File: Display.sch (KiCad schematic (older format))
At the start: 16 parts, among them Q1 Q_NPN_BCE, Q2 Q_NPN_BCE, U1 74LS47, U5 DA56-11GWA

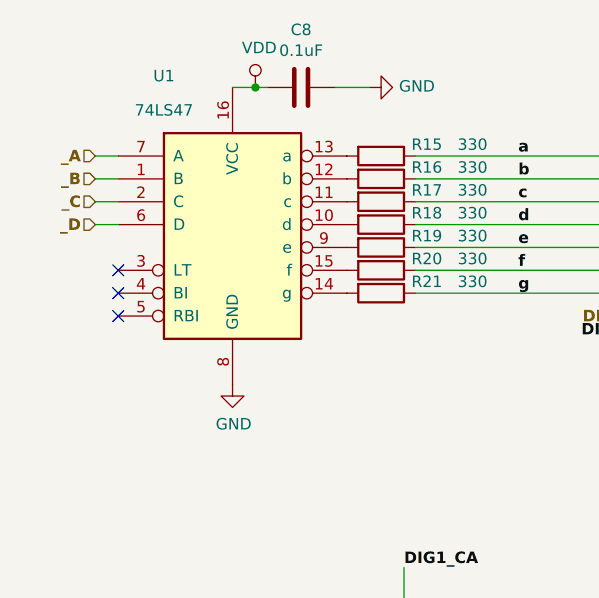
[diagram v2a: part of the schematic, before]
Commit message: Se agregan recomendaciones izq->dcha (In/Out), se Reorganiza jerarquía y bus de datos, se coloca graphics lines para indicar submodulos
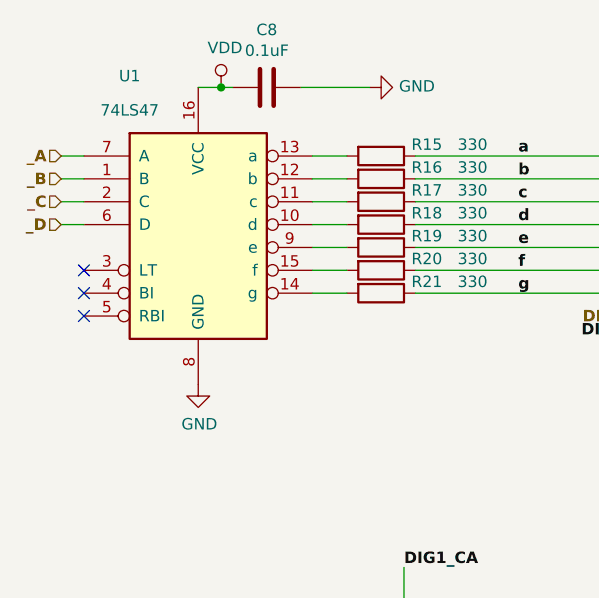
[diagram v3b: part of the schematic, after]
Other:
- moved on the sheet: C8, U1
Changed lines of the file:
@@
 $Descr A4 11693 8268
 encoding utf-8
-Sheet 4 4
+Sheet 2 4
 Title "Kit Development for MCU PIC"
 Date "2019-05-14"
@@
 L 74xx:74LS47 U1
 U 1 1 5CDD9840
-P 3950 2950
-F 0 "U1" H 3650 3600 50  0000 C CNN
-F 1 "74LS47" H 3650 3450 50  0000 C CNN
-F 2 "" H 3950 2950 50  0001 C CNN
-F 3 "http://www.ti.com/lit/gpn/sn74LS47" H 3950 2950 50  0001 C CNN
-	1    3950 2950
+P 3800 2950
+AR Path="/5CCF70C1/5CDD9840" Ref="U1"  Part="1"
+AR Path="/5CFF2978/5CDD9840" Ref="U?"  Part="1"
+AR Path="/5D021BAF/5CDD9840" Ref="U?"  Part="1"
+F 0 "U1" H 3500 3600 50  0000 C CNN
+F 1 "74LS47" H 3500 3450 50  0000 C CNN
+F 2 "" H 3800 2950 50  0001 C CNN
+F 3 "http://www.ti.com/lit/gpn/sn74LS47" H 3800 2950 50  0001 C CNN
+	1    3800 2950
 	1    0    0    -1
 $EndComp
@@
 U 1 1 5CDDBAB7
 P 6450 3050
+AR Path="/5CCF70C1/5CDDBAB7" Ref="U5"  Part="1"
+AR Path="/5CFF2978/5CDDBAB7" Ref="U?"  Part="1"
+AR Path="/5D021BAF/5CDDBAB7" Ref="U?"  Part="1"
 F 0 "U5" H 6450 3717 50  0000 C CNN
 F 1 "DA56-11GWA" H 6450 3626 50  0000 C CNN
@@
 U 1 1 5CDE018E
 P 4600 2650
+AR Path="/5CCF70C1/5CDE018E" Ref="R15"  Part="1"
+AR Path="/5CFF2978/5CDE018E" Ref="R?"  Part="1"
+AR Path="/5D021BAF/5CDE018E" Ref="R?"  Part="1"
 F 0 "R15" V 4550 2850 50  0000 C CNN
 F 1 "330" V 4550 3050 50  0000 C CNN
@@
 U 1 1 5CDEB3B9
 P 4600 2750
+AR Path="/5CCF70C1/5CDEB3B9" Ref="R16"  Part="1"
+AR Path="/5CFF2978/5CDEB3B9" Ref="R?"  Part="1"
+AR Path="/5D021BAF/5CDEB3B9" Ref="R?"  Part="1"
 F 0 "R16" V 4550 2950 50  0000 C CNN
 F 1 "330" V 4550 3150 50  0000 C CNN
@@
 U 1 1 5CDEB627
 P 4600 2850
+AR Path="/5CCF70C1/5CDEB627" Ref="R17"  Part="1"
+AR Path="/5CFF2978/5CDEB627" Ref="R?"  Part="1"
+AR Path="/5D021BAF/5CDEB627" Ref="R?"  Part="1"
 F 0 "R17" V 4550 3050 50  0000 C CNN
 F 1 "330" V 4550 3250 50  0000 C CNN
@@
 U 1 1 5CDEB79B
 P 4600 2950
+AR Path="/5CCF70C1/5CDEB79B" Ref="R18"  Part="1"
+AR Path="/5CFF2978/5CDEB79B" Ref="R?"  Part="1"
+AR Path="/5D021BAF/5CDEB79B" Ref="R?"  Part="1"
 F 0 "R18" V 4550 3150 50  0000 C CNN
 F 1 "330" V 4550 3350 50  0000 C CNN
@@
 U 1 1 5CDEB915
 P 4600 3050
+AR Path="/5CCF70C1/5CDEB915" Ref="R19"  Part="1"
+AR Path="/5CFF2978/5CDEB915" Ref="R?"  Part="1"
+AR Path="/5D021BAF/5CDEB915" Ref="R?"  Part="1"
 F 0 "R19" V 4550 3250 50  0000 C CNN
 F 1 "330" V 4550 3450 50  0000 C CNN
@@
 U 1 1 5CDEBA36
 P 4600 3150
+AR Path="/5CCF70C1/5CDEBA36" Ref="R20"  Part="1"
+AR Path="/5CFF2978/5CDEBA36" Ref="R?"  Part="1"
+AR Path="/5D021BAF/5CDEBA36" Ref="R?"  Part="1"
 F 0 "R20" V 4550 3350 50  0000 C CNN
 F 1 "330" V 4550 3550 50  0000 C CNN
@@
 U 1 1 5CDEBB90
 P 4600 3250
+AR Path="/5CCF70C1/5CDEBB90" Ref="R21"  Part="1"
+AR Path="/5CFF2978/5CDEBB90" Ref="R?"  Part="1"
+AR Path="/5D021BAF/5CDEBB90" Ref="R?"  Part="1"
 F 0 "R21" V 4550 3450 50  0000 C CNN
 F 1 "330" V 4550 3650 50  0000 C CNN
@@
 L power:GND #PWR019
 U 1 1 5CDF0B85
-P 3950 3650
-F 0 "#PWR019" H 3950 3400 50  0001 C CNN
-F 1 "GND" H 3955 3477 50  0000 C CNN
-F 2 "" H 3950 3650 50  0001 C CNN
-F 3 "" H 3950 3650 50  0001 C CNN
-	1    3950 3650
+P 3800 3650
+AR Path="/5CCF70C1/5CDF0B85" Ref="#PWR019"  Part="1"
+AR Path="/5CFF2978/5CDF0B85" Ref="#PWR?"  Part="1"
+AR Path="/5D021BAF/5CDF0B85" Ref="#PWR?"  Part="1"
+F 0 "#PWR019" H 3800 3400 50  0001 C CNN
+F 1 "GND" H 3805 3477 50  0000 C CNN
+F 2 "" H 3800 3650 50  0001 C CNN
+F 3 "" H 3800 3650 50  0001 C CNN
+	1    3800 3650
 	1    0    0    -1
 $EndComp
@@
 U 1 1 5CDFE125
 P 6600 4800
+AR Path="/5CCF70C1/5CDFE125" Ref="Q2"  Part="1"
+AR Path="/5CFF2978/5CDFE125" Ref="Q?"  Part="1"
+AR Path="/5D021BAF/5CDFE125" Ref="Q?"  Part="1"
 F 0 "Q2" H 6791 4846 50  0000 L CNN
 F 1 "Q_NPN_BCE" H 6791 4755 50  0000 L CNN
@@
 U 1 1 5CDFE12F
 P 6150 4800
+AR Path="/5CCF70C1/5CDFE12F" Ref="R22"  Part="1"
+AR Path="/5CFF2978/5CDFE12F" Ref="R?"  Part="1"
+AR Path="/5D021BAF/5CDFE12F" Ref="R?"  Part="1"
 F 0 "R22" V 6050 4750 50  0000 C CNN
 F 1 "1K" V 6050 4900 50  0000 C CNN
@@
 U 1 1 5CDFE144
 P 6350 5400
+AR Path="/5CCF70C1/5CDFE144" Ref="#PWR022"  Part="1"
+AR Path="/5CFF2978/5CDFE144" Ref="#PWR?"  Part="1"
+AR Path="/5D021BAF/5CDFE144" Ref="#PWR?"  Part="1"
 F 0 "#PWR022" H 6350 5150 50  0001 C CNN
 F 1 "GND" H 6355 5227 50  0000 C CNN
@@
 Text Label 5800 3450 2    50   ~ 10
 DIG1_CA
-Text HLabel 3350 2650 0    50   Input ~ 10
+Text HLabel 3200 2650 0    50   Input ~ 10
 _A
-Text HLabel 3350 2750 0    50   Input ~ 10
+Text HLabel 3200 2750 0    50   Input ~ 10
 _B
-Text HLabel 3350 2850 0    50   Input ~ 10
+Text HLabel 3200 2850 0    50   Input ~ 10
 _C
-Text HLabel 3350 2950 0    50   Input ~ 10
+Text HLabel 3200 2950 0    50   Input ~ 10
 _D
 Text HLabel 5900 4800 0    50   Input ~ 10
@@
 AR Path="/5CCEA06C/5CE3EAA0" Ref="#PWR?"  Part="1"
 AR Path="/5CCF70C1/5CE3EAA0" Ref="#PWR021"  Part="1"
+AR Path="/5CFF2978/5CE3EAA0" Ref="#PWR?"  Part="1"
+AR Path="/5D021BAF/5CE3EAA0" Ref="#PWR?"  Part="1"
 F 0 "#PWR021" H 4550 2100 50  0001 C CNN
 F 1 "GND" V 4555 2222 50  0000 R CNN
@@
 	0    -1   -1   0
 $EndComp
-Wire Wire Line
-	4400 2350 4550 2350
 $Comp
 L Device:C C?
 U 1 1 5CE3EAA7
-P 4250 2350
+P 4100 2350
 AR Path="/5CCEA06C/5CE3EAA7" Ref="C?"  Part="1"
 AR Path="/5CCF70C1/5CE3EAA7" Ref="C8"  Part="1"
-F 0 "C8" V 3998 2350 50  0000 C CNN
-F 1 "0.1uF" V 4089 2350 50  0000 C CNN
-F 2 "" H 4288 2200 50  0001 C CNN
-F 3 "~" H 4250 2350 50  0001 C CNN
-	1    4250 2350
+AR Path="/5CFF2978/5CE3EAA7" Ref="C?"  Part="1"
+AR Path="/5D021BAF/5CE3EAA7" Ref="C?"  Part="1"
+F 0 "C8" V 3848 2350 50  0000 C CNN
+F 1 "0.1uF" V 3939 2350 50  0000 C CNN
+F 2 "" H 4138 2200 50  0001 C CNN
+F 3 "~" H 4100 2350 50  0001 C CNN
+	1    4100 2350
 	0    1    1    0
 $EndComp
@@
 U 1 1 5CDFE13A
 P 6350 5100
+AR Path="/5CCF70C1/5CDFE13A" Ref="R23"  Part="1"
+AR Path="/5CFF2978/5CDFE13A" Ref="R?"  Part="1"
+AR Path="/5D021BAF/5CDFE13A" Ref="R?"  Part="1"
 F 0 "R23" V 6250 5050 50  0000 C CNN
 F 1 "10K" V 6250 5200 50  0000 C CNN
@@
 U 1 1 5CD2B4DB
 P 4600 4800
+AR Path="/5CCF70C1/5CD2B4DB" Ref="Q1"  Part="1"
+AR Path="/5CFF2978/5CD2B4DB" Ref="Q?"  Part="1"
+AR Path="/5D021BAF/5CD2B4DB" Ref="Q?"  Part="1"
 F 0 "Q1" H 4791 4846 50  0000 L CNN
 F 1 "Q_NPN_BCE" H 4791 4755 50  0000 L CNN
@@
 U 1 1 5CD2B4E5
 P 4150 4800
+AR Path="/5CCF70C1/5CD2B4E5" Ref="R13"  Part="1"
+AR Path="/5CFF2978/5CD2B4E5" Ref="R?"  Part="1"
+AR Path="/5D021BAF/5CD2B4E5" Ref="R?"  Part="1"
 F 0 "R13" V 4050 4750 50  0000 C CNN
 F 1 "1K" V 4050 4900 50  0000 C CNN
@@
 U 1 1 5CD2B4F0
 P 4250 5400
+AR Path="/5CCF70C1/5CD2B4F0" Ref="#PWR020"  Part="1"
+AR Path="/5CFF2978/5CD2B4F0" Ref="#PWR?"  Part="1"
+AR Path="/5D021BAF/5CD2B4F0" Ref="#PWR?"  Part="1"
 F 0 "#PWR020" H 4250 5150 50  0001 C CNN
 F 1 "GND" H 4255 5227 50  0000 C CNN
@@
 U 1 1 5CD2B4FC
 P 4350 5100
+AR Path="/5CCF70C1/5CD2B4FC" Ref="R14"  Part="1"
+AR Path="/5CFF2978/5CD2B4FC" Ref="R?"  Part="1"
+AR Path="/5D021BAF/5CD2B4FC" Ref="R?"  Part="1"
 F 0 "R14" V 4250 5050 50  0000 C CNN
 F 1 "10K" V 4250 5200 50  0000 C CNN
@@
 Wire Wire Line
 	4700 5000 4700 5350
-NoConn ~ 3450 3150
-NoConn ~ 3450 3250
-NoConn ~ 3450 3350
+NoConn ~ 3300 3150
+NoConn ~ 3300 3250
+NoConn ~ 3300 3350
 NoConn ~ 7050 3350
 Wire Wire Line
@@
 L power:VDD #PWR0120
 U 1 1 5CF6D9AF
-P 4050 2350
-F 0 "#PWR0120" H 4050 2200 50  0001 C CNN
-F 1 "VDD" H 4067 2523 50  0000 C CNN
-F 2 "" H 4050 2350 50  0001 C CNN
-F 3 "" H 4050 2350 50  0001 C CNN
-	1    4050 2350
-	1    0    0    -1
-$EndComp
-Wire Wire Line
-	3450 2650 3350 2650
-Wire Wire Line
-	3450 2750 3350 2750
-Wire Wire Line
-	3450 2850 3350 2850
-Wire Wire Line
-	3450 2950 3350 2950
+P 3900 2350
+AR Path="/5CCF70C1/5CF6D9AF" Ref="#PWR0120"  Part="1"
+AR Path="/5CFF2978/5CF6D9AF" Ref="#PWR?"  Part="1"
+AR Path="/5D021BAF/5CF6D9AF" Ref="#PWR?"  Part="1"
+F 0 "#PWR0120" H 3900 2200 50  0001 C CNN
+F 1 "VDD" H 3917 2523 50  0000 C CNN
+F 2 "" H 3900 2350 50  0001 C CNN
+F 3 "" H 3900 2350 50  0001 C CNN
+	1    3900 2350
+	1    0    0    -1
+$EndComp
+Wire Wire Line
+	3300 2650 3200 2650
+Wire Wire Line
+	3300 2750 3200 2750
+Wire Wire Line
+	3300 2850 3200 2850
+Wire Wire Line
+	3300 2950 3200 2950
 Wire Wire Line
 	4350 5400 4250 5400
 Wire Wire Line
-	3950 2350 4050 2350
-Wire Wire Line
-	4050 2350 4100 2350
-Connection ~ 4050 2350
+	3800 2350 3900 2350
+Wire Wire Line
+	3900 2350 3950 2350
+Connection ~ 3900 2350
+Wire Wire Line
+	4250 2350 4550 2350
+Wire Wire Line
+	4450 2650 4300 2650
+Wire Wire Line
+	4450 2750 4300 2750
+Wire Wire Line
+	4450 2850 4300 2850
+Wire Wire Line
+	4450 2950 4300 2950
+Wire Wire Line
+	4450 3050 4300 3050
+Wire Wire Line
+	4450 3150 4300 3150
+Wire Wire Line
+	4450 3250 4300 3250
 $EndSCHEMATC

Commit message: Se agrega ubicación de componentes, asociación de footprint, pendiente Ruteo.
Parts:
- C8: footprint (none) -> Capacitor_SMD:C_0603_1608Metric; PArt Number (none) -> 732-7939-1-ND
- Q1, Q2: footprint (none) -> Package_TO_SOT_SMD:SOT-23
- R13, R14, R15, R16, R17, R18, R19, R20, R21, R22, R23: footprint (none) -> Resistor_SMD:R_0603_1608Metric_Pad1.05x0.95mm_HandSolder
- U1: footprint (none) -> Package_DIP:DIP-16_W7.62mm
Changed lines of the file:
@@
 F 0 "U1" H 3500 3600 50  0000 C CNN
 F 1 "74LS47" H 3500 3450 50  0000 C CNN
-F 2 "" H 3800 2950 50  0001 C CNN
+F 2 "Package_DIP:DIP-16_W7.62mm" H 3800 2950 50  0001 C CNN
 F 3 "http://www.ti.com/lit/gpn/sn74LS47" H 3800 2950 50  0001 C CNN
 	1    3800 2950
@@
 F 0 "R15" V 4550 2850 50  0000 C CNN
 F 1 "330" V 4550 3050 50  0000 C CNN
-F 2 "" V 4530 2650 50  0001 C CNN
+F 2 "Resistor_SMD:R_0603_1608Metric_Pad1.05x0.95mm_HandSolder" V 4530 2650 50  0001 C CNN
 F 3 "~" H 4600 2650 50  0001 C CNN
 	1    4600 2650
@@
 F 0 "R16" V 4550 2950 50  0000 C CNN
 F 1 "330" V 4550 3150 50  0000 C CNN
-F 2 "" V 4530 2750 50  0001 C CNN
+F 2 "Resistor_SMD:R_0603_1608Metric_Pad1.05x0.95mm_HandSolder" V 4530 2750 50  0001 C CNN
 F 3 "~" H 4600 2750 50  0001 C CNN
 	1    4600 2750
@@
 F 0 "R17" V 4550 3050 50  0000 C CNN
 F 1 "330" V 4550 3250 50  0000 C CNN
-F 2 "" V 4530 2850 50  0001 C CNN
+F 2 "Resistor_SMD:R_0603_1608Metric_Pad1.05x0.95mm_HandSolder" V 4530 2850 50  0001 C CNN
 F 3 "~" H 4600 2850 50  0001 C CNN
 	1    4600 2850
@@
 F 0 "R18" V 4550 3150 50  0000 C CNN
 F 1 "330" V 4550 3350 50  0000 C CNN
-F 2 "" V 4530 2950 50  0001 C CNN
+F 2 "Resistor_SMD:R_0603_1608Metric_Pad1.05x0.95mm_HandSolder" V 4530 2950 50  0001 C CNN
 F 3 "~" H 4600 2950 50  0001 C CNN
 	1    4600 2950
@@
 F 0 "R19" V 4550 3250 50  0000 C CNN
 F 1 "330" V 4550 3450 50  0000 C CNN
-F 2 "" V 4530 3050 50  0001 C CNN
+F 2 "Resistor_SMD:R_0603_1608Metric_Pad1.05x0.95mm_HandSolder" V 4530 3050 50  0001 C CNN
 F 3 "~" H 4600 3050 50  0001 C CNN
 	1    4600 3050
@@
 F 0 "R20" V 4550 3350 50  0000 C CNN
 F 1 "330" V 4550 3550 50  0000 C CNN
-F 2 "" V 4530 3150 50  0001 C CNN
+F 2 "Resistor_SMD:R_0603_1608Metric_Pad1.05x0.95mm_HandSolder" V 4530 3150 50  0001 C CNN
 F 3 "~" H 4600 3150 50  0001 C CNN
 	1    4600 3150
@@
 F 0 "R21" V 4550 3450 50  0000 C CNN
 F 1 "330" V 4550 3650 50  0000 C CNN
-F 2 "" V 4530 3250 50  0001 C CNN
+F 2 "Resistor_SMD:R_0603_1608Metric_Pad1.05x0.95mm_HandSolder" V 4530 3250 50  0001 C CNN
 F 3 "~" H 4600 3250 50  0001 C CNN
 	1    4600 3250
@@
 F 0 "Q2" H 6791 4846 50  0000 L CNN
 F 1 "Q_NPN_BCE" H 6791 4755 50  0000 L CNN
-F 2 "" H 6800 4900 50  0001 C CNN
+F 2 "Package_TO_SOT_SMD:SOT-23" H 6800 4900 50  0001 C CNN
 F 3 "~" H 6600 4800 50  0001 C CNN
 	1    6600 4800
@@
 F 0 "R22" V 6050 4750 50  0000 C CNN
 F 1 "1K" V 6050 4900 50  0000 C CNN
-F 2 "" V 6080 4800 50  0001 C CNN
+F 2 "Resistor_SMD:R_0603_1608Metric_Pad1.05x0.95mm_HandSolder" V 6080 4800 50  0001 C CNN
 F 3 "~" H 6150 4800 50  0001 C CNN
 	1    6150 4800
@@
 F 0 "C8" V 3848 2350 50  0000 C CNN
 F 1 "0.1uF" V 3939 2350 50  0000 C CNN
-F 2 "" H 4138 2200 50  0001 C CNN
+F 2 "Capacitor_SMD:C_0603_1608Metric" H 4138 2200 50  0001 C CNN
 F 3 "~" H 4100 2350 50  0001 C CNN
+F 4 "732-7939-1-ND" V 4100 2350 50  0001 C CNN "PArt Number"
 	1    4100 2350
 	0    1    1    0
@@
 F 0 "R23" V 6250 5050 50  0000 C CNN
 F 1 "10K" V 6250 5200 50  0000 C CNN
-F 2 "" V 6280 5100 50  0001 C CNN
+F 2 "Resistor_SMD:R_0603_1608Metric_Pad1.05x0.95mm_HandSolder" V 6280 5100 50  0001 C CNN
 F 3 "~" H 6350 5100 50  0001 C CNN
 	1    6350 5100
@@
 F 0 "Q1" H 4791 4846 50  0000 L CNN
 F 1 "Q_NPN_BCE" H 4791 4755 50  0000 L CNN
-F 2 "" H 4800 4900 50  0001 C CNN
+F 2 "Package_TO_SOT_SMD:SOT-23" H 4800 4900 50  0001 C CNN
 F 3 "~" H 4600 4800 50  0001 C CNN
 	1    4600 4800
@@
 F 0 "R13" V 4050 4750 50  0000 C CNN
 F 1 "1K" V 4050 4900 50  0000 C CNN
-F 2 "" V 4080 4800 50  0001 C CNN
+F 2 "Resistor_SMD:R_0603_1608Metric_Pad1.05x0.95mm_HandSolder" V 4080 4800 50  0001 C CNN
 F 3 "~" H 4150 4800 50  0001 C CNN
 	1    4150 4800
@@
 F 0 "R14" V 4250 5050 50  0000 C CNN
 F 1 "10K" V 4250 5200 50  0000 C CNN
-F 2 "" V 4280 5100 50  0001 C CNN
+F 2 "Resistor_SMD:R_0603_1608Metric_Pad1.05x0.95mm_HandSolder" V 4280 5100 50  0001 C CNN
 F 3 "~" H 4350 5100 50  0001 C CNN
 	1    4350 5100

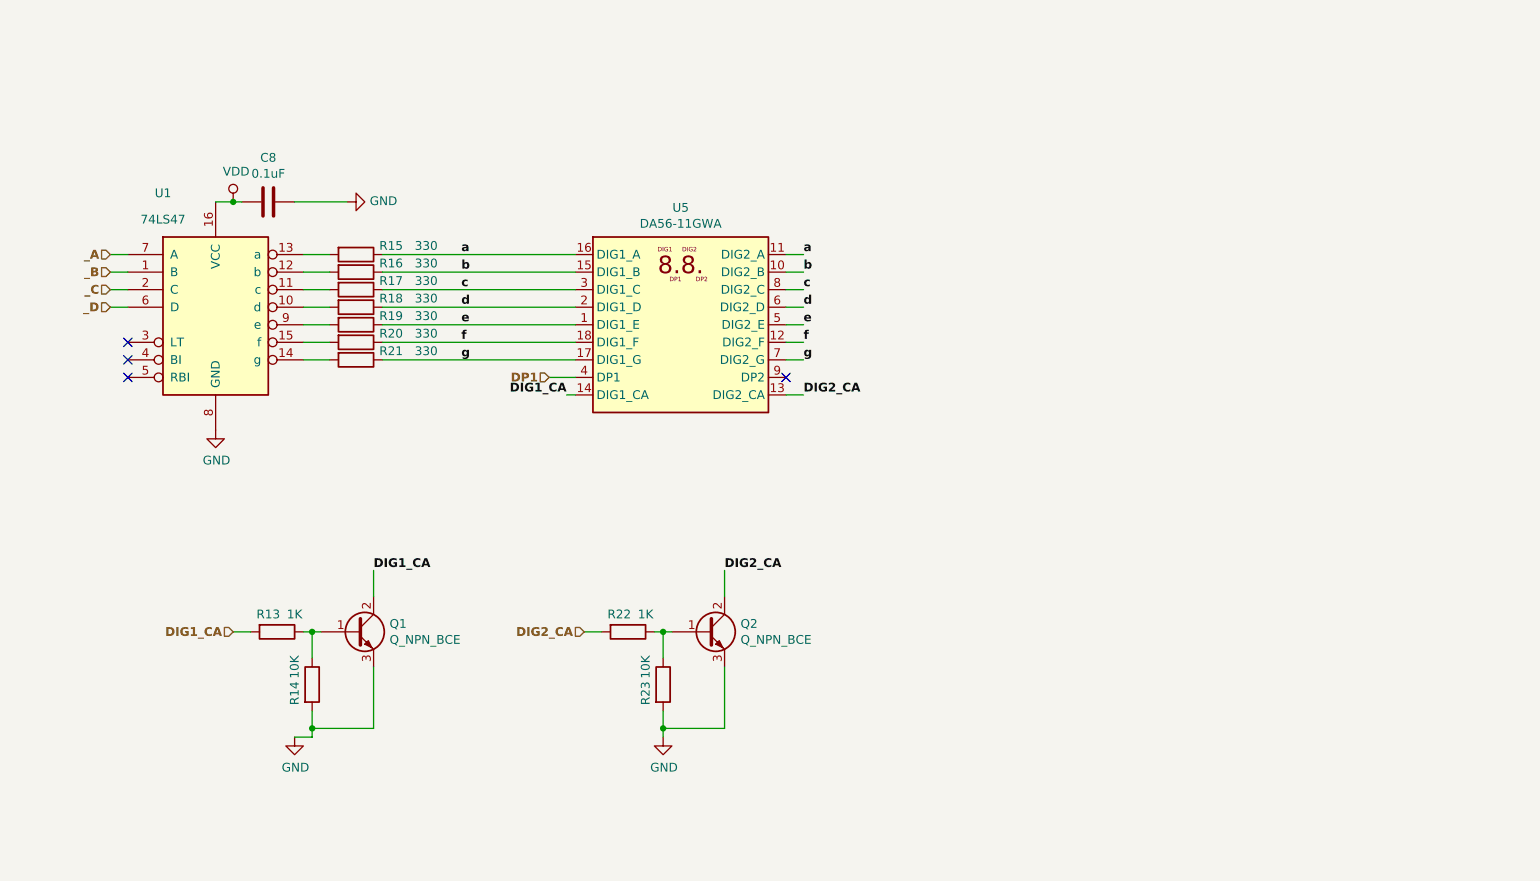
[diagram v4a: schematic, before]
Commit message: Se agrega recomendaciones  de jacobo salvador
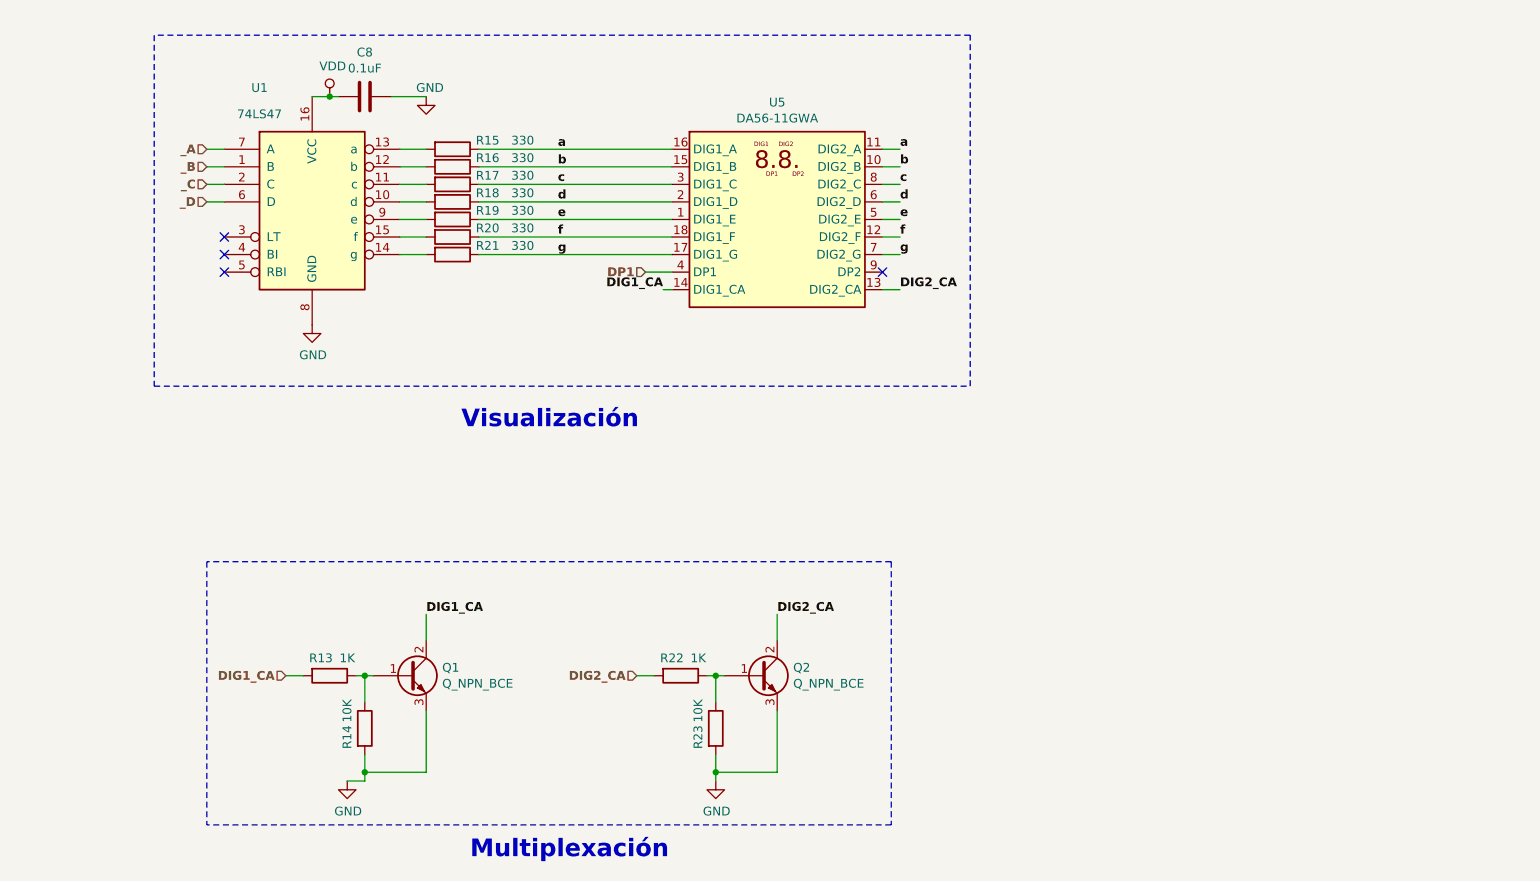
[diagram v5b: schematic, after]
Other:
- note added: "Multiplexación"
- note added: "Visualización"
- moved on the sheet: C8, Q1, Q2, R13, R14, R15, R16, R17, R18, R19, R20, R21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
